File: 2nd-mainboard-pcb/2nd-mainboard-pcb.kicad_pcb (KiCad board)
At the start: 4 copper layers, 99 x 97.5 mm, 131 parts, among them J1 PJ-082BH, J10 Servo Motor BL Touch, J11 T3, J12 Steckverbinder_Male_Fans, J13 Steckverbinder_Female_Leistung, J14 FAN3, J15 Steckverbinder_Female_Motoren, J16 ISP, J18 Quartz, J19 T2, J2 Fan_12/5V_Regelung, J20 T2, J21 T2, J22 T3, J23 Conn_01x04_Socket, J24 Steckverbinder_Male_Leistung, J3 Fan_12/5V_Regelung, J4 FAN0, J5 FAN1, J6 FAN2, J7 Stepper Motor, J8 Servo Motor SM, J9 Microstepping, P1 USB_C_Receptacle_USB2.0_14P, SW3 PTS820 J25K SMTR LFS, U1 SQJ409EP-T1_GE3, U10 ATmega328PB-A, U12 MPU-6050, U2 SZ1SMB5927BT3G, U3 TPS56837HRPAR, U4 TPS565208, U5 FT232RL, U7 TPM16050-S6TR, U8 RJK0456DPB-00-J5, U9 RJK0456DPB-00-J5, Y1 ECS-160-18-4X-CKM

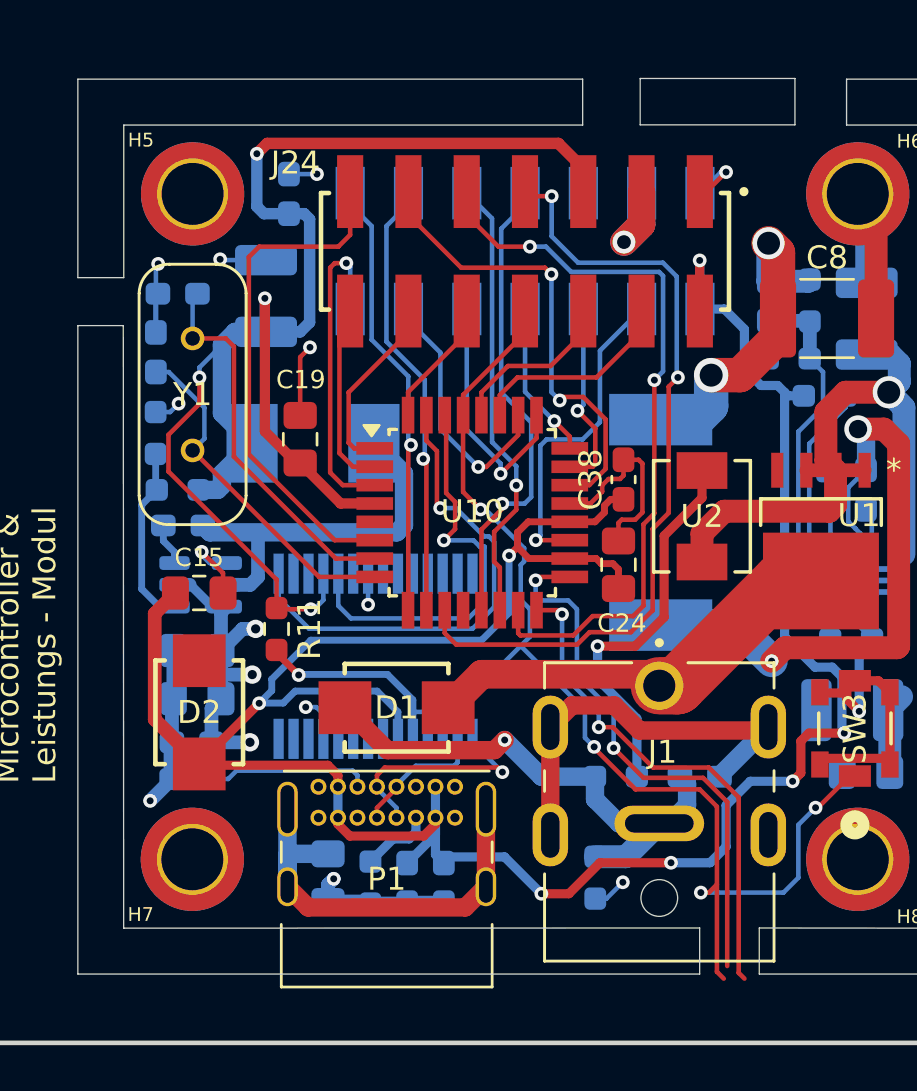
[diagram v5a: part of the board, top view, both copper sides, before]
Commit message: 5v flaeche, aref eingestellt, jetzt on top flaechen angehen
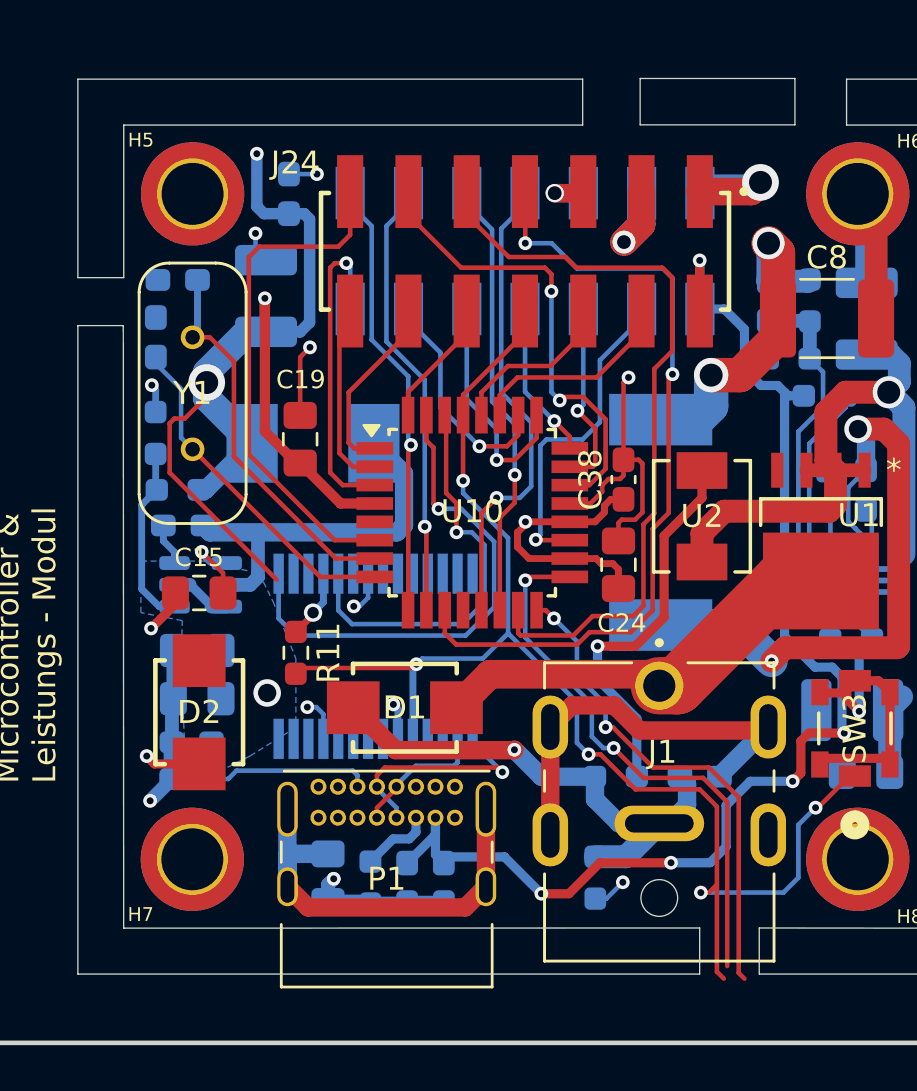
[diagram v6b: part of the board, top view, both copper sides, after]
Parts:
- moved R11 1.33 mm to (110.0, 133.0)
- moved C21 0.65 mm to (103.9, 119.2)
- moved C22 0.60 mm to (104.8, 116.8)
- moved D1 0.36 mm to (114.8, 135.4)
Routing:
- net AREF: track 118.4 -> 81.7 mm, vias 7 -> 9
- net +5V_POW: track 69.9 -> 53.2 mm, vias 4 -> 5
- net +12V: track 34.0 -> 22.8 mm, vias 6 -> 4
- net RESET: track 63.8 -> 61.1 mm
- net GND: track 77.8 -> 79.2 mm
- net ADC3: track 11.3 -> 10.0 mm
- net TXD: track 21.5 -> 22.3 mm
- net ADC2: track 11.0 -> 10.3 mm
- net GND2: track 23.0 -> 22.3 mm
- net RXD: track 18.4 -> 17.9 mm
- net MOSI: track 32.4 -> 33.0 mm, vias 2 -> 0
- added copper zone on B.Cu, net +12V
- added copper zone on In2.Cu, net AREF

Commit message: layout backup vor drehung
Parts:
- moved C19 1.76 mm to (109.7, 125.4), turned to -90 degrees
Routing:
- net +5V_POW: track 53.2 -> 22.5 mm, vias 5 -> 4
- net Quartz_2: track 17.0 -> 18.4 mm
- net LED_MOT0: track 22.3 -> 23.7 mm
- net Quartz_1: track 14.9 -> 16.2 mm
- net GND: track 79.2 -> 80.0 mm, vias 13 -> 12
